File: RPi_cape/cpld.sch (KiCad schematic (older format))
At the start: 65 parts, among them J15 Conn_02x05_Odd_Even, Q10 MMBT3904, Q9 MMBT3904, U29 LP5907MFX-3.3, U30 LP5907MFX-1.8, U31 5M40ZE64, U32 MIC1557, U33 5M80ZT100 / 5M240ZT100

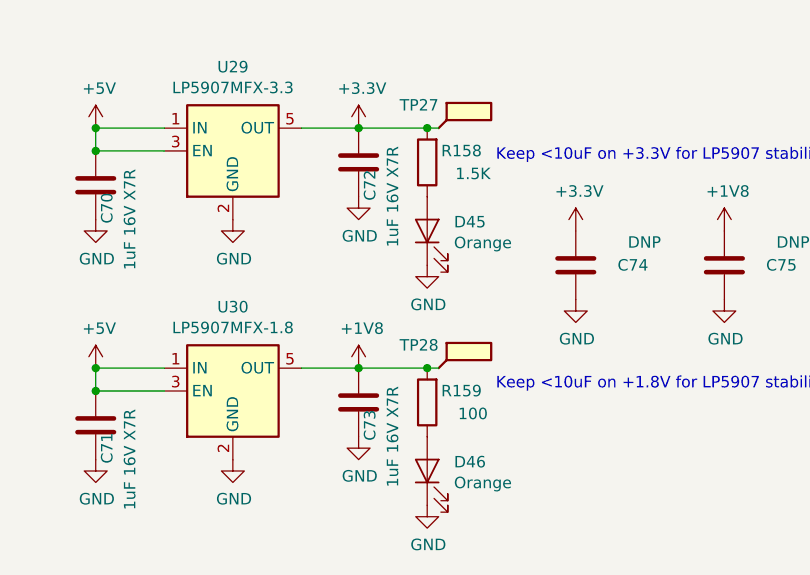
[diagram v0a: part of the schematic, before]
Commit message: Extra info, post-design-review fixes
Added extra info on existing alternate circuit options
Added extra info on parts selection
Created initial PCB file
Added bulk cap to +5V input
Design review fixes:
Moved Raspberry Pi PWM output to GPIO18 to take advantage of hardware PWM
Fixed floating shutdown input on audio amp
Added series resistor R177 to allow low battery output to signal to both CPLD and external LED at the same time
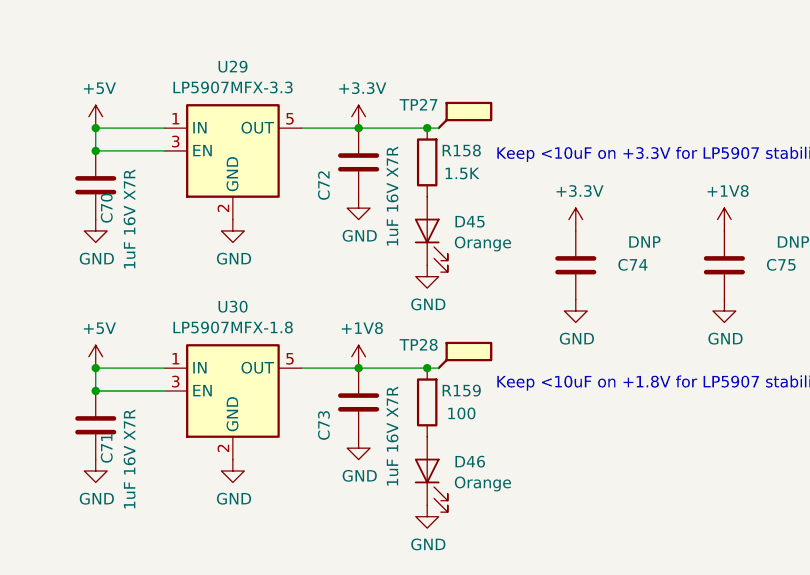
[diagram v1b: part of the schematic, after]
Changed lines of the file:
@@
 AR Path="/5E8DEDC0/5F062AA9" Ref="C?"  Part="1"
 AR Path="/5E8C8865/5F062AA9" Ref="C72"  Part="1"
-F 0 "C72" V 2500 8900 50  0000 C CNN
+F 0 "C72" V 2700 8900 50  0000 C CNN
 F 1 "1uF 16V X7R" V 2400 8950 50  0000 C CNN
 F 2 "Capacitor_SMD:C_0805_2012Metric" H 2588 8650 50  0001 C CNN
@@
 AR Path="/5E8DEDC0/5F066087" Ref="C?"  Part="1"
 AR Path="/5E8C8865/5F066087" Ref="C73"  Part="1"
-F 0 "C73" V 2500 9950 50  0000 C CNN
+F 0 "C73" V 2700 9950 50  0000 C CNN
 F 1 "1uF 16V X7R" V 2400 10000 50  0000 C CNN
 F 2 "Capacitor_SMD:C_0805_2012Metric" H 2588 9700 50  0001 C CNN
@@
 AR Path="/5E8C8865/5F6F670A" Ref="R159"  Part="1"
 F 0 "R159" H 2700 9800 50  0000 C CNN
-F 1 "100" H 2650 9900 50  0000 C CNN
+F 1 "100" H 2700 9900 50  0000 C CNN
 F 2 "Resistor_SMD:R_1206_3216Metric" V 2780 9850 50  0001 C CNN
 F 3 "~" H 2850 9850 50  0001 C CNN
@@
 AR Path="/5E8C8865/5F70646F" Ref="R158"  Part="1"
 F 0 "R158" H 2700 8750 50  0000 C CNN
-F 1 "1.5K" H 2650 8850 50  0000 C CNN
+F 1 "1.5K" H 2700 8850 50  0000 C CNN
 F 2 "Resistor_SMD:R_1206_3216Metric" V 2780 8800 50  0001 C CNN
 F 3 "~" H 2850 8800 50  0001 C CNN

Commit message: Finished schematic, most of PCB placement
Added error budget for analog inputs
Finished most of PCB placement and started routing
Added R185, R186 to allow powering CPLD from alarm power for better power-down alarm sound flexibility
Changed power-down alarm monitoring from +5VD to +3.3V, and put +5VA and +24VA monitoring as DNP by default, to match the CPLD's ability to run off backup battery and monitor +5VA/+24VA
Moved from 3x AA (4.5V) to 4x AA (6V) alarm battery for better audio voltage, and added PNP diode-ORing circuit (Q12 etc.) to accomodate higher voltage, changed low-battery threshold to 5V
Added pull-down resistors to sensor op-amp outputs to help extend low-end output range
Changed 1nF, 10nF, 100nF caps to 0603-size for better fit of CPLD decoupling caps
Added additional bulk cap C19 to audio amp's supply just in case of alarm-induced supply fluctuations
Decreased CPLD's I2C pull-up values to deal with anticipated PCB capacitance etc.
Removed additional dual-op-amp footprint option on analog inputs, due to high availability of single op-amps
Adjusted O2 sensor input clamping to reduce errors from diode leakage current (changed from zener to low-leakage clamps to rails)
Changed O2 sensor op-amp to different lower-offset part to reduce total error from +/- 4.2% FS to +/- 1.7% FS
Fixed missing power section for U17
Added rotary encoder input
Consolidated +5VA fuse options
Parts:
- added R185: 0, Resistor_SMD:R_1206_3216Metric, symbol Device:R
- added R186: DNP, Resistor_SMD:R_1206_3216Metric, symbol Device:R
- C76, C77, C78, C80, C81, C82, C83, C87, C89, C90, C91, C92, C93, C94, C95: footprint Capacitor_SMD:C_0805_2012Metric -> Capacitor_SMD:C_0603_1608Metric; Part Number 08055C104KAT2A -> 06035C104JAT2A
- C79: footprint Capacitor_SMD:C_0805_2012Metric -> Capacitor_SMD:C_0603_1608Metric; Manufacturer Kemet -> AVX; Part Number C0805C102J5GACTU -> 06035A102JAT2A
- R155, R156: value 10K -> 3.3K
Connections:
- net +5V: now also R186.2; no longer C70.2, C71.2, U29.1 (IN), U29.3 (EN), U30.1 (IN), U30.3 (EN)
- new net: C70.2, C71.2, R185.1, R186.1, U29.1 (IN), U29.3 (EN), U30.1 (IN), U30.3 (EN)
- new net +BATT: R185.2
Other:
- note added: "CPLD can be powered from backup battery when\nmain 5V power is out"

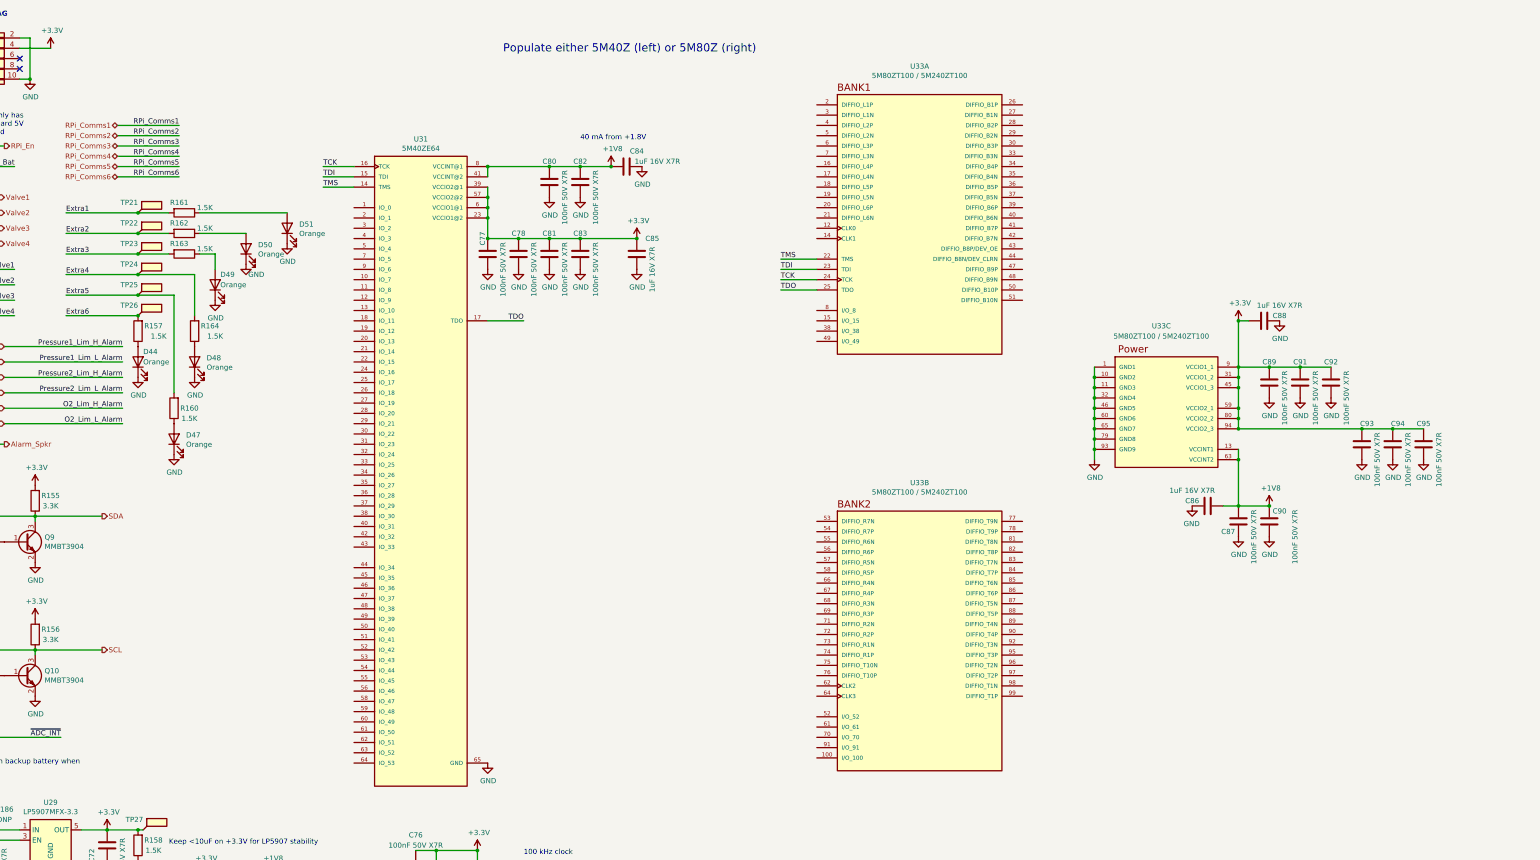
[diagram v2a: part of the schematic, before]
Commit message: Finished layout, minor design changes
Assigned CPLD pins
Finished routing PCB
Moved rotary encoder inputs to CPLD
Removed separate decoupling caps for smaller CPLD footprint due to routing constraints
Added pull-downs on CPLD inputs for each valve driver (R198 etc.)
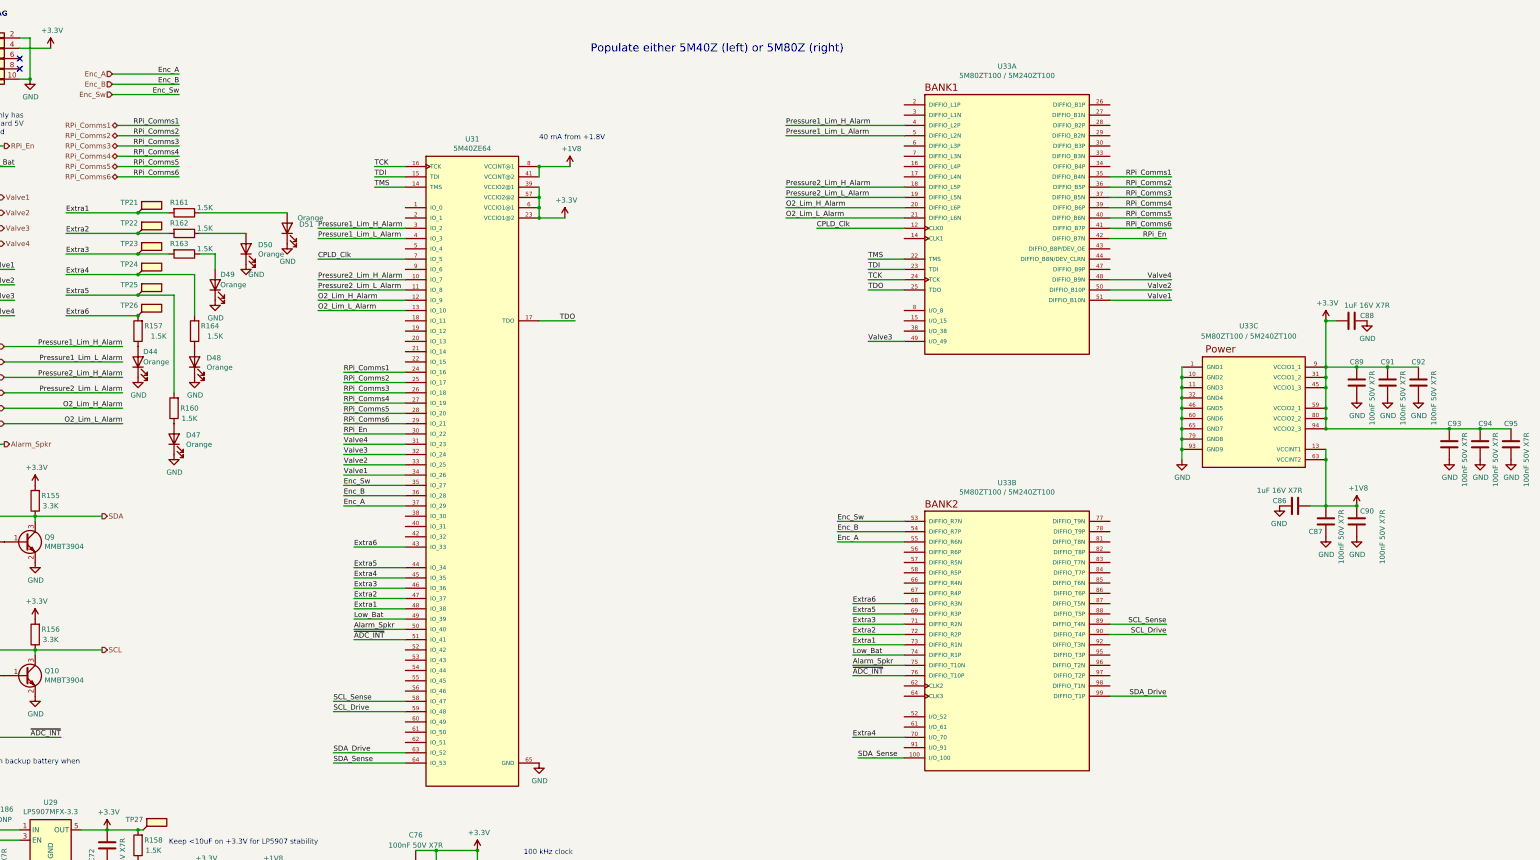
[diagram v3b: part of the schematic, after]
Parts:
- removed C77, C78, C80, C81, C82, C83: 100nF 50V X7R, Capacitor_SMD:C_0603_1608Metric, symbol Device:C
- removed C84, C85: 1uF 16V X7R, Capacitor_SMD:C_0805_2012Metric, symbol Device:C
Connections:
- net Alarm_Spkr: now also U31.50 (IO_40), U33.75 (DIFFIO_T10N)
- net CPLD_Clk: now also U31.7 (IO_5), U33.12 (CLK0)
- net Extra1: now also U31.48 (IO_38), U33.73 (DIFFIO_R1N)
- net Extra2: now also U31.47 (IO_37), U33.72 (DIFFIO_R2P)
- net Extra3: now also U31.46 (IO_36), U33.71 (DIFFIO_R2N)
- net Extra4: now also U31.45 (IO_35), U33.70 (I/O_70)
- net Extra5: now also U31.44 (IO_34), U33.69 (DIFFIO_R3P)
- net Extra6: now also U31.43 (IO_33), U33.68 (DIFFIO_R3N)
- net Low_Bat: now also U31.49 (IO_39), U33.74 (DIFFIO_R1P)
- net O2_Lim_H_Alarm: now also U31.12 (IO_9), U33.20 (DIFFIO_L6P)
- net O2_Lim_L_Alarm: now also U31.13 (IO_10), U33.21 (DIFFIO_L6N)
- net Pressure1_Lim_H_Alarm: now also U31.3 (IO_2), U33.4 (DIFFIO_L2P)
- net Pressure1_Lim_L_Alarm: now also U31.4 (IO_3), U33.5 (DIFFIO_L2N)
- net Pressure2_Lim_H_Alarm: now also U31.10 (IO_7), U33.18 (DIFFIO_L5P)
- net Pressure2_Lim_L_Alarm: now also U31.11 (IO_8), U33.19 (DIFFIO_L5N)
- net RPi_Comms1: now also U31.24 (IO_16), U33.35 (DIFFIO_B4N)
- net RPi_Comms2: now also U31.25 (IO_17), U33.36 (DIFFIO_B5P)
- net RPi_Comms3: now also U31.26 (IO_18), U33.37 (DIFFIO_B5N)
- net RPi_Comms4: now also U31.27 (IO_19), U33.39 (DIFFIO_B6P)
- net RPi_Comms5: now also U31.28 (IO_20), U33.40 (DIFFIO_B6N)
- net RPi_Comms6: now also U31.29 (IO_21), U33.41 (DIFFIO_B7P)
- net RPi_En: now also U31.30 (IO_22), U33.42 (DIFFIO_B7N)
- net SCL: now also U31.58 (IO_47), U33.89 (DIFFIO_T4N)
- net SCL_Drive: now also U31.59 (IO_48), U33.90 (DIFFIO_T4P)
- net SDA: now also U31.64 (IO_53), U33.100 (I/O_100)
- net SDA_Drive: now also U31.63 (IO_52), U33.99 (DIFFIO_T1P)
- net Valve1: now also U31.34 (IO_26), U33.51 (DIFFIO_B10N)
- net Valve2: now also U31.33 (IO_25), U33.50 (DIFFIO_B10P)
- net Valve3: now also U31.32 (IO_24), U33.49 (I/O_49)
- net Valve4: now also U31.31 (IO_23), U33.48 (DIFFIO_B9N)
- net ~ADC_INT: now also U31.51 (IO_41), U33.76 (DIFFIO_T10P)
- net Enc_Sw: now reaches U31.35 (IO_27)
- net Enc_Sw: now also U33.53 (DIFFIO_R7N)
- net Enc_B: now reaches U31.36 (IO_28)
- net Enc_B: now also U33.54 (DIFFIO_R7P)
- net Enc_A: now reaches U31.37 (IO_29)
- net Enc_A: now also U33.55 (DIFFIO_R6N)
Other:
- moved on the sheet: C86, C87, C88, C89, C90, C91, C92, C93, C94, C95, U31, U33A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
